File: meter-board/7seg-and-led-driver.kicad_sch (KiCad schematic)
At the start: 0 parts

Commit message: update circuits
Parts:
- added C19, C20, C21, C22: 0.1u, ProjectEV_Capacitor:C_1005M, symbol ProjectEV_Capacitor:C_1005M
- added R118, R119, R120, R121, R122, R123, R124, R125: 220, my_Resistor:R_0603_1608M, symbol my_Resistor:R_0603_1608M
- added R126, R127, R128, R129, R130, R131, R132, R133, R134, R135, R136, R137, R138, R139, R140, R141, R142, R143, R144, R145, R146, R147, R148, R149, R150, R151, R152: 100k, my_Resistor:R_0402_1005M, symbol my_Resistor:R_0402_1005M
- added U21, U22, U23: SN74HC595BRWNR, my_Logic:SN74HC595BRWNR, symbol my_Logic:SN74HC595BRWNR
- added U24: TBD62783AFNG,EL, my_PMIC:TBD62783AFNG,EL, symbol my_PMIC:TBD62783AFNG,EL
- added U25, U26: TBD62183AFNG,EL, my_PMIC:TBD62183AFNG,EL, symbol my_PMIC:TBD62183AFNG,EL
- added U27: SN74LV4T125RGYR, my_Logic:SN74LV4T125RGYR, symbol my_Logic:SN74LV4T125RGYR
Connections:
- new net: R142.1, U23.7 (QH), U26.1 (I1)
- new net: R143.1, U23.6 (QG), U26.2 (I2)
- new net: R144.1, U23.5 (QF), U26.3 (I3)
- new net: R145.1, U23.4 (QE), U26.4 (I4)
- new net: R146.1, U23.3 (QD), U26.5 (I5)
- new net: R147.1, U23.2 (QC), U26.6 (I6)
- new net: R148.1, U23.1 (QB), U26.7 (I7)
- new net: R149.1, U23.15 (QA), U26.8 (I8)
- new net: R131.1, U21.2 (QC), U24.6 (I6)
- new net: R126.1, U21.7 (QH), U24.1 (I1)
- new net: R140.1, U22.1 (QB), U25.7 (I7)
- new net: U21.11 (SRCLK), U22.11 (SRCLK), U23.11 (SRCLK), U27.3
- new net: U21.12 (RCLK), U22.12 (RCLK), U23.12 (RCLK), U27.6
- new net: U21.9 (QH'), U22.14 (SER)
- new net: R141.1, U22.15 (QA), U25.8 (I8)
- new net: R139.1, U22.2 (QC), U25.6 (I6)
- new net: R138.1, U22.3 (QD), U25.5 (I5)
- new net: R137.1, U22.4 (QE), U25.4 (I4)
- new net: R136.1, U22.5 (QF), U25.3 (I3)
- new net: R135.1, U22.6 (QG), U25.2 (I2)
- new net: R134.1, U22.7 (QH), U25.1 (I1)
- new net: U22.9 (QH'), U23.14 (SER)
- new net: U21.14 (SER), U27.8
- new net: R122.1, U24.14 (O5)
- new net: R119.1, U24.17 (O2)
- new net: R128.1, U21.5 (QF), U24.3 (I3)
- new net: R125.1, U24.11 (O8)
- new net: R120.1, U24.16 (O3)
- new net: R118.1, U24.18 (O1)
- new net: R124.1, U24.12 (O7)
- new net: R123.1, U24.13 (O6)
- new net: R121.1, U24.15 (O4)
- new net: R127.1, U21.6 (QG), U24.2 (I2)
- new net: R129.1, U21.4 (QE), U24.4 (I4)
- new net: R130.1, U21.3 (QD), U24.5 (I5)
- new net: R132.1, U21.1 (QB), U24.7 (I7)
- new net: R133.1, U21.15 (QA), U24.8 (I8)
- new net +5VD: C19.1, C20.1, C21.1, C22.1, U21.10 (~{SRCLR}), U21.16 (VCC), U22.10 (~{SRCLR}), U22.16 (VCC), U23.10 (~{SRCLR}), U23.16 (VCC), U24.9 (VCC), U27.14 (VCC)
- new net 7seg_A: R125.2
- new net 7seg_B: R124.2
- new net 7seg_C: R123.2
- new net 7seg_CC1: U25.11 (O8)
- new net 7seg_CC2: U25.12 (O7)
- new net 7seg_CC3: U25.13 (O6)
- new net 7seg_CC4: U25.14 (O5)
- new net 7seg_CC5: U25.15 (O4)
- new net 7seg_CC6: U25.16 (O3)
- new net 7seg_D: R122.2
- new net 7seg_DP: R118.2
- new net 7seg_E: R121.2
- new net 7seg_F: R120.2
- new net 7seg_G: R119.2
- new net CLK: R150.1, U27.2
- new net GND: C19.2, C20.2, C21.2, C22.2, R126.2, R127.2, R128.2, R129.2, R130.2, R131.2, R132.2, R133.2, R134.2, R135.2, R136.2, R137.2, R138.2, R139.2, R140.2, R141.2, R142.2, R143.2, R144.2, R145.2, R146.2, R147.2, R148.2, R149.2, R150.2, R151.2, R152.2, U21.13 (~{OE}), U21.17 (PAD), U21.8 (GND), U22.13 (~{OE}), U22.17 (PAD), U22.8 (GND), U23.13 (~{OE}), U23.17 (PAD), U23.8 (GND), U24.10 (GND), U25.9 (GND), U26.9 (GND), U27.1, U27.10, U27.12, U27.13, U27.15 (PAD), U27.4, U27.7 (GND)
- new net MOSI: R152.1, U27.9
- new net RGB_B: U26.18 (O1)
- new net RGB_G: U26.17 (O2)
- new net RGB_R: U26.16 (O3)
- new net W5_W1: U26.11 (O8)
- new net W5_W2: U26.12 (O7)
- new net W5_W3: U26.13 (O6)
- new net W5_W4: U26.14 (O5)
- new net W5_W5: U26.15 (O4)
- new net ~{CS}: R151.1, U27.5
- no-connect marks 0 -> 6

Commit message: modify label
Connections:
- net W5_W5 renamed R1_R1
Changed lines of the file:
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@@
+		)
+	)
+	(hierarchical_label "R1_R1"
+		(shape output)
+		(at 391.16 137.16 0)
+		(effects
+			(font
+				(size 1.27 1.27)
+			)
+			(justify left)
 		)
 	)
@@
 		(effects
 			(font
-				(size 1.27 1.27)
-			)
-			(justify left)
-		)
-	)
-	(hierarchical_label "W5_W5"
-		(shape output)
-		(at 391.16 137.16 0)
-		(effects
-			(font

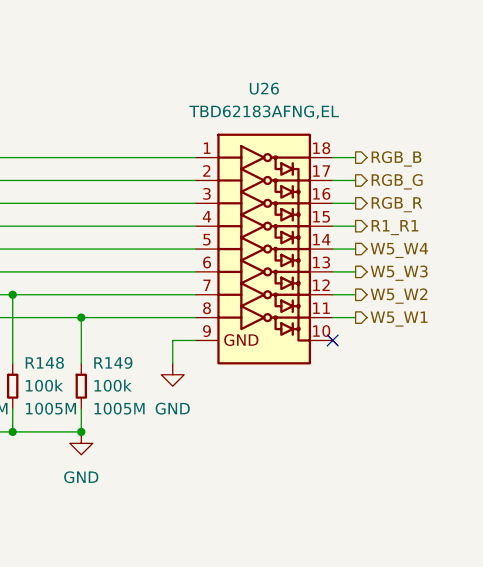
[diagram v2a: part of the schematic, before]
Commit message: modify net name
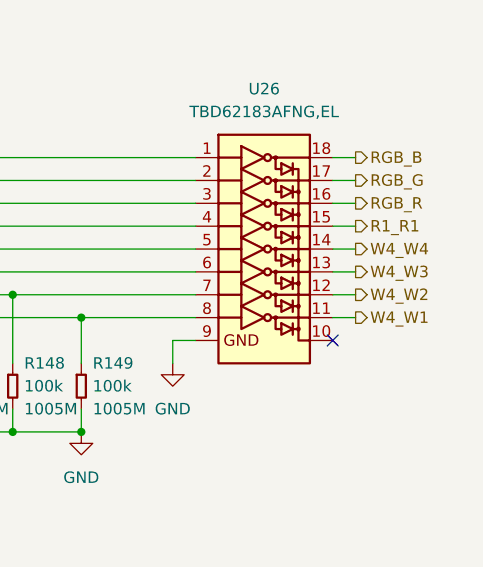
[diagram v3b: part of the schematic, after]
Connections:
- net W5_W1 renamed W4_W1
- net W5_W2 renamed W4_W2
- net W5_W3 renamed W4_W3
- net W5_W4 renamed W4_W4
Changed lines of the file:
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@@
 		)
 	)
-	(hierarchical_label "W5_W1"
+	(hierarchical_label "W4_W1"
 		(shape output)
 		(at 391.16 147.32 0)
@@
 		)
 	)
-	(hierarchical_label "W5_W4"
+	(hierarchical_label "W4_W4"
 		(shape output)
 		(at 391.16 139.7 0)
@@
 		)
 	)
-	(hierarchical_label "W5_W2"
+	(hierarchical_label "W4_W2"
 		(shape output)
 		(at 391.16 144.78 0)
@@
 		)
 	)
-	(hierarchical_label "W5_W3"
+	(hierarchical_label "W4_W3"
 		(shape output)
 		(at 391.16 142.24 0)
